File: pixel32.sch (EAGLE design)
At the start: 68 parts, among them CON1 DS1066-07M-SIDE, CON2 DS1066-07M-SIDE, CON3 PINHEAD_1X02-2.54, CON4 PINHEAD_1X01-2.54, CON5 PINHEAD_1X01-2.54, CON6 PINHEAD_1X01-2.54, CON7 PINHEAD_1X01-2.54, IC1 STM32F030K6TX-LQFP32(7X7), IC3 ST3485SOIC8, IC6 MC74VHC1GT125, IC7 MC74VHC1GT125, IC8 LM317

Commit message: blah
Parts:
- added PAD3: WIREPADSMD2.5-1.8, valenok_master_library:WIREPADSMD2.5-1.8
- added U$3: CONNECTION, usb2can_master_lib:CONNECTION
- PAD1, PAD2, PAD4: BOM (none) -> EXCLUDE
- R10: device rc:R-0805 -> rc:R-0603
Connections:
- net CLOCK_BUFFERED: now also RN2.3; no longer RN2.2
- net GND: now also U$3.P$2
- net GNDD: now also U$3.P$1
- net N$15: now also RN2.6; no longer RN2.7
- net VDD_3V3: now also PAD3.P
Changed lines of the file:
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@@
 <attribute name="BOM" x="124.46" y="137.16" size="1.778" layer="96" rot="R180" display="off"/>
 </instance>
-<instance part="TP3" gate="G$1" x="121.92" y="116.84" rot="R180">
-<attribute name="PARTNO" x="121.92" y="116.84" size="1.778" layer="96" rot="R180" display="off"/>
-<attribute name="BOM" x="121.92" y="116.84" size="1.778" layer="96" rot="R180" display="off"/>
+<instance part="TP3" gate="G$1" x="124.46" y="116.84" rot="R180">
+<attribute name="PARTNO" x="124.46" y="116.84" size="1.778" layer="96" rot="R180" display="off"/>
+<attribute name="BOM" x="124.46" y="116.84" size="1.778" layer="96" rot="R180" display="off"/>
 </instance>
 <instance part="Q1" gate="G$1" x="137.16" y="129.54"/>
 <instance part="FRAME1" gate="G$1" x="0" y="0"/>
 <instance part="C1" gate="G$1" x="152.4" y="142.24" rot="R90"/>
-<instance part="TP4" gate="G$1" x="121.92" y="101.6">
-<attribute name="PARTNO" x="121.92" y="101.6" size="1.778" layer="96" display="off"/>
-<attribute name="BOM" x="121.92" y="101.6" size="1.778" layer="96" display="off"/>
-</instance>
-<instance part="GND2" gate="1" x="111.76" y="96.52" rot="MR0"/>
+<instance part="TP4" gate="G$1" x="124.46" y="101.6">
+<attribute name="PARTNO" x="124.46" y="101.6" size="1.778" layer="96" display="off"/>
+<attribute name="BOM" x="124.46" y="101.6" size="1.778" layer="96" display="off"/>
+</instance>
+<instance part="GND2" gate="1" x="114.3" y="96.52" rot="MR0"/>
 </instances>
 <busses>
@@
 <segment>
 <pinref part="GND2" gate="1" pin="GND"/>
-<wire x1="111.76" y1="99.06" x2="111.76" y2="101.6" width="0.1524" layer="91"/>
+<wire x1="114.3" y1="99.06" x2="114.3" y2="101.6" width="0.1524" layer="91"/>
 <pinref part="TP4" gate="G$1" pin="P$1"/>
-<wire x1="111.76" y1="101.6" x2="114.3" y2="101.6" width="0.1524" layer="91"/>
+<wire x1="114.3" y1="101.6" x2="116.84" y2="101.6" width="0.1524" layer="91"/>
 </segment>
 </net>
@@
 <junction x="142.24" y="116.84"/>
 <pinref part="TP3" gate="G$1" pin="P$1"/>
-<wire x1="137.16" y1="116.84" x2="129.54" y2="116.84" width="0.1524" layer="91"/>
+<wire x1="137.16" y1="116.84" x2="132.08" y2="116.84" width="0.1524" layer="91"/>
 <pinref part="Q1" gate="G$1" pin="S"/>
 <wire x1="137.16" y1="124.46" x2="137.16" y2="116.84" width="0.1524" layer="91"/>
@@
 <part name="GND19" library="supply_symbols" deviceset="GND" device="" value="GND"/>
 <part name="+P16" library="supply_symbols" deviceset="24V" device=""/>
-<part name="R10" library="rc" deviceset="R" device="-0805"/>
+<part name="R10" library="rc" deviceset="R" device="-0603"/>
 <part name="R13" library="rc" deviceset="R" device="-0603"/>
 <part name="GND37" library="supply_symbols" deviceset="GND" device="" value="GND"/>
@@
 </part>
 <part name="+P17" library="supply_symbols" deviceset="3.3V" device=""/>
-<part name="PAD1" library="valenok_master_library" deviceset="WIREPAD" device="SMD2.5-1.8"/>
-<part name="PAD2" library="valenok_master_library" deviceset="WIREPAD" device="SMD2.5-1.8"/>
-<part name="PAD4" library="valenok_master_library" deviceset="WIREPAD" device="SMD2.5-1.8"/>
+<part name="PAD1" library="valenok_master_library" deviceset="WIREPAD" device="SMD2.5-1.8">
+<attribute name="BOM" value="EXCLUDE"/>
+</part>
+<part name="PAD2" library="valenok_master_library" deviceset="WIREPAD" device="SMD2.5-1.8">
+<attribute name="BOM" value="EXCLUDE"/>
+</part>
+<part name="PAD4" library="valenok_master_library" deviceset="WIREPAD" device="SMD2.5-1.8">
+<attribute name="BOM" value="EXCLUDE"/>
+</part>
 <part name="GND9" library="supply_symbols" deviceset="GNDD" device="" value="GNDD"/>
 <part name="CON4" library="pinhead" deviceset="PINHEAD_1X01" device="-2.54"/>
@@
 <part name="+P18" library="supply_symbols" deviceset="3.3V" device=""/>
 <part name="U$1" library="logo" deviceset="RTU" device=""/>
+<part name="U$3" library="usb2can_master_lib" deviceset="CONNECTION" device=""/>
+<part name="PAD3" library="valenok_master_library" deviceset="WIREPAD" device="SMD2.5-1.8">
+<attribute name="BOM" value="EXCLUDE"/>
+</part>
 </parts>
 <sheets>
@@
 </instance>
 <instance part="+P17" gate="G$1" x="137.16" y="231.14" rot="MR0"/>
-<instance part="PAD1" gate="G$1" x="129.54" y="220.98"/>
-<instance part="PAD2" gate="G$1" x="132.08" y="208.28" rot="R90"/>
-<instance part="PAD4" gate="G$1" x="132.08" y="198.12" rot="R90"/>
+<instance part="PAD1" gate="G$1" x="129.54" y="220.98">
+<attribute name="BOM" x="129.54" y="220.98" size="1.778" layer="96" display="off"/>
+</instance>
+<instance part="PAD2" gate="G$1" x="132.08" y="208.28" rot="R90">
+<attribute name="BOM" x="132.08" y="208.28" size="1.778" layer="96" rot="R90" display="off"/>
+</instance>
+<instance part="PAD4" gate="G$1" x="132.08" y="198.12" rot="R90">
+<attribute name="BOM" x="132.08" y="198.12" size="1.778" layer="96" rot="R90" display="off"/>
+</instance>
 <instance part="GND9" gate="G$1" x="160.02" y="160.02" rot="MR0"/>
 <instance part="CON4" gate="G$1" x="96.52" y="139.7" rot="R270"/>
@@
 <instance part="CON7" gate="G$1" x="119.38" y="139.7" rot="R270"/>
 <instance part="+P18" gate="G$1" x="109.22" y="190.5"/>
-<instance part="U$1" gate="G$1" x="302.26" y="134.62"/>
+<instance part="U$1" gate="G$1" x="373.38" y="63.5"/>
+<instance part="U$3" gate="G$1" x="335.28" y="167.64" rot="MR0"/>
+<instance part="PAD3" gate="G$1" x="129.54" y="228.6">
+<attribute name="BOM" x="129.54" y="228.6" size="1.778" layer="96" display="off"/>
+</instance>
 </instances>
 <busses>
@@
 <wire x1="139.7" y1="228.6" x2="137.16" y2="228.6" width="0.1524" layer="91"/>
 <wire x1="137.16" y1="228.6" x2="137.16" y2="231.14" width="0.1524" layer="91"/>
+<pinref part="PAD3" gate="G$1" pin="P"/>
+<wire x1="137.16" y1="228.6" x2="132.08" y2="228.6" width="0.1524" layer="91"/>
+<junction x="137.16" y="228.6"/>
 </segment>
 <segment>
@@
 <pinref part="GND44" gate="1" pin="GND"/>
 <wire x1="330.2" y1="165.1" x2="330.2" y2="162.56" width="0.1524" layer="91"/>
+<wire x1="330.2" y1="165.1" x2="330.2" y2="167.64" width="0.1524" layer="91"/>
+<junction x="330.2" y="165.1"/>
+<pinref part="U$3" gate="G$1" pin="P$2"/>
+<wire x1="332.74" y1="167.64" x2="330.2" y2="167.64" width="0.1524" layer="91"/>
 </segment>
 <segment>
@@
 <segment>
 <pinref part="CON2" gate="G$1" pin="5"/>
-<wire x1="327.66" y1="182.88" x2="340.36" y2="182.88" width="0.1524" layer="91"/>
-<pinref part="RN2" gate="G$1" pin="7"/>
+<pinref part="RN2" gate="G$1" pin="6"/>
+<wire x1="330.2" y1="182.88" x2="340.36" y2="182.88" width="0.1524" layer="91"/>
+<wire x1="327.66" y1="180.34" x2="330.2" y2="180.34" width="0.1524" layer="91"/>
+<wire x1="330.2" y1="180.34" x2="330.2" y2="182.88" width="0.1524" layer="91"/>
 </segment>
 </net>
@@
 <pinref part="CON2" gate="G$1" pin="6"/>
 <pinref part="RN2" gate="G$1" pin="5"/>
-<wire x1="330.2" y1="180.34" x2="340.36" y2="180.34" width="0.1524" layer="91"/>
-<wire x1="327.66" y1="177.8" x2="330.2" y2="177.8" width="0.1524" layer="91"/>
-<wire x1="330.2" y1="177.8" x2="330.2" y2="180.34" width="0.1524" layer="91"/>
+<wire x1="332.74" y1="180.34" x2="340.36" y2="180.34" width="0.1524" layer="91"/>
+<wire x1="327.66" y1="177.8" x2="332.74" y2="177.8" width="0.1524" layer="91"/>
+<wire x1="332.74" y1="177.8" x2="332.74" y2="180.34" width="0.1524" layer="91"/>
 </segment>
 </net>
 <net name="CLOCK_BUFFERED" class="0">
 <segment>
-<wire x1="314.96" y1="182.88" x2="312.42" y2="182.88" width="0.1524" layer="91"/>
-<label x="312.42" y="182.88" size="1.27" layer="95" rot="R180" xref="yes"/>
-<pinref part="RN2" gate="G$1" pin="2"/>
+<label x="309.88" y="182.88" size="1.27" layer="95" rot="R180" xref="yes"/>
+<pinref part="RN2" gate="G$1" pin="3"/>
+<wire x1="312.42" y1="182.88" x2="309.88" y2="182.88" width="0.1524" layer="91"/>
+<wire x1="314.96" y1="180.34" x2="312.42" y2="180.34" width="0.1524" layer="91"/>
+<wire x1="312.42" y1="180.34" x2="312.42" y2="182.88" width="0.1524" layer="91"/>
 </segment>
 <segment>
@@
 <pinref part="U$6" gate="G$1" pin="P$1"/>
 <wire x1="340.36" y1="165.1" x2="337.82" y2="165.1" width="0.1524" layer="91"/>
-</segment>
-<segment>
+<pinref part="U$3" gate="G$1" pin="P$1"/>
+<wire x1="337.82" y1="167.64" x2="340.36" y2="167.64" width="0.1524" layer="91"/>
+<wire x1="340.36" y1="167.64" x2="340.36" y2="165.1" width="0.1524" layer="91"/>
+<junction x="340.36" y="165.1"/>
+</segment>
+<segment>

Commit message: -pixel32 update
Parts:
- removed FRAME1: RTU_A4, frames:RTU_A4
- removed FRAME2: RTU_A3, frames:RTU_A3
- added CON10, CON11, CON8, CON9: PINHEAD_1X01-2.54, pinhead:PINHEAD_1X01-2.54
- added CON12: PINHEAD_1X02-2.54, pinhead:PINHEAD_1X02-2.54
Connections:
- net GND: now also CON12.2, CON3.2
- net N$10: now also CON9.1
- net N$21: now also CON10.1
- net N$23: now also CON11.1
- net TEMP: now also CON12.1; no longer R8.2
- net VDD_24V: now also CON8.1
- net VDD_3V3: now also R8.2; no longer CON3.2
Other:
- moved on the sheet: C26, CON3, R8

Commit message: -pixel32 update
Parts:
- removed U$1: RTU, logo:RTU
- added D5: SMBJ26CA-SMB, ExitControl_v2_master_library:SMBJ26CA-SMB
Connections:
- net GND: now also CON12.1, CON3.1, D5.A; no longer CON12.2, CON3.2, R8.1
- net TEMP: now also CON12.2, CON3.2, R8.1; no longer CON12.1, CON3.1
- net VDD_24V: now also D5.C
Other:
- moved on the sheet: C1, C2, C26, C3, C4, C5, CON1, CON2, IC8, MODULE1, R6, R7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

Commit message: -more edge connectors
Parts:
- added CON13, CON14: PINHEAD_1X07-2, pinhead:PINHEAD_1X07-2
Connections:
- net GNDD: now also CON13.1, CON14.1
- net N$11: now also CON13.4
- net N$12: now also CON13.3
- net N$13: now also CON13.2
- net N$14: now also CON14.4
- net N$15: now also CON14.3
- net N$19: now also CON14.2
- net RS485_A: now also CON13.6, CON14.6
- net RS485_B: now also CON13.5, CON14.5
- net VDD_24V: now also CON13.7, CON14.7
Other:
- moved on the sheet: CON1, CON2, D5

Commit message: voltage regulator recalculated, minor fixes, attributes
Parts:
- removed Z1: 16MHz, watchdog_master_library:CRYSTAL-3.2X2.5-4P
- added C6: 100 nF, rc:C-0603
- added Y1: 16MHz, crystals:CRYSTAL-3.2X2.5-4P
- C1, C16, C2, C3, C4: FARNELL# (none) -> 2496930
- C13, C17, C18, C23, C24, C26: FARNELL# (none) -> 2496834
- C14: FARNELL# (none) -> 2496917
- C15: FARNELL# (none) -> 2496827
- C19, C20: value (none) -> 10 pF; FARNELL# (none) -> 1414601
- C21: value 0.1uF -> 100 nF; FARNELL# (none) -> 2496834
- C5: value (none) -> 10 uF
- CON1, CON2: value DS1066-07M-SIDE -> B7B-PH-K-S-SIDE; device pixel_masterlib:DS1066-07M-SIDE -> pixel_masterlib:B7B-PH-K-S-SIDE
- D5: value SMBJ26CA-SMB -> TVS_DIODE-SMB; device ExitControl_v2_master_library:SMBJ26CA-SMB -> pixel_masterlib:TVS_DIODE-SMB; CHIPDIP (none) -> 8023193826; DIGIKEY# (none) -> 497-15658-2-ND; FARNELL# (none) -> 1749366; MANF (none) -> STMicroelectronics; MANF# (none) -> SMBJ26CA; TME# (none) -> SMBJ26CA
- IC8: device masterlib:LM317 -> pixel_masterlib:LM317
- LED2: CHIPDIP (none) -> 8598509892; FARNELL# (none) -> 2293494; TME# (none) -> LTST-C191KGKT
- LED_ANODE, LED_CATHODE1, LED_CATHODE2, LED_CATHODE3: value WIREPADSMD5-2,5 -> WIREPADSMD2.5-1.8; device valenok_master_library:WIREPADSMD5-2,5 -> wirepad:WIREPADSMD2.5-1.8
- MODULE1: device ali_modules:GW1584 -> pixel_masterlib:GW1584
- PAD1, PAD2, PAD3, PAD4: device valenok_master_library:WIREPADSMD2.5-1.8 -> wirepad:WIREPADSMD2.5-1.8
- R1, R2: ASSY DO NOT PLACE -> DO NOT MOUNT
- R11, R12: FARNELL# (none) -> 2303059
- R14, R15, R8, R9: FARNELL# (none) -> 2008341
- R39: FARNELL# (none) -> 2303145
- R5: FARNELL# (none) -> 2303067
- R6: device rc:R-0805 -> rc:R-0603; FARNELL# (none) -> 2303145
- R7: value 5K6 -> 1K6; device rc:R-0805 -> rc:R-0603; FARNELL# (none) -> 2303159
- SJ1, SJ2, SJ3, SJ4: BOM (none) -> EXCLUDE
- TP1, TP2, TP3, TP4: device pixhawk2:PAD.05 -> misc:PAD.05
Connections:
- net GND: now also C6.1, Y1.GND; no longer Z1.GND
- net N$4: now also Y1.1; no longer Z1.1
- net N$5: now also C6.2
- net N$9: now also Y1.2; no longer Z1.2
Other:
- note added: "10 uF 50V in 1812 packagage is unavailable"
- note added: "Crystal load capacitance is 9 pF, otherwise recalculate C19 and C20"
- note added: "Do not mount"
- note added: "No 510 Ohm resistor arrays are available on Farnell nor TME"
- note added: "R1, R2 are for software version definition"
- note added: "R10, R13 are not defined"
- note added: "RGB LED SINGLE CHANNEL"
- note removed: "Do not use"
- note removed: "R1, R2, R3 are for software version definition"
- note removed: "RGB LED RED CHANNEL"
- moved on the sheet: C19, C20, C21, C23, C24, C26, C5, CON1, CON12, CON2, CON3, D1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

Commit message: input sense divider values added boot0 fix
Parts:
- added R3: 20K, rc:R-0603
- R10: value (none) -> 100K
- R13: value (none) -> 10K
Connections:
- new net N$6: IC1.PB8, R3.1
- net GND: now also R3.2
- net N$3: now also R3.2
- net PWM: now also R3.1

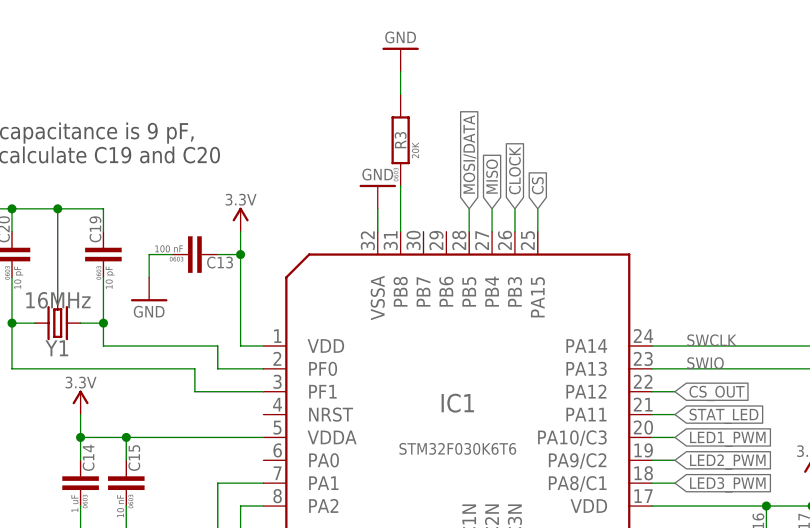
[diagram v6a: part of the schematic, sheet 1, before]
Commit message: TME part numbers added
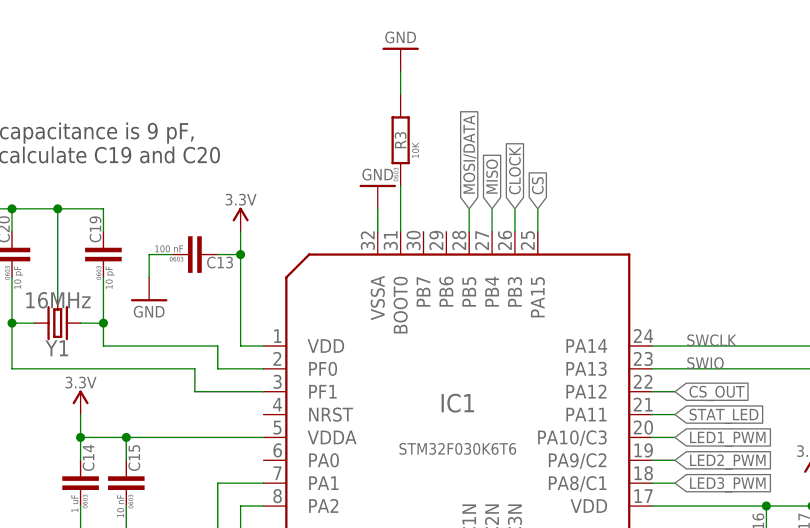
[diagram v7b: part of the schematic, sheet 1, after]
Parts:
- C1, C16, C2, C3, C4: TME# (none) -> GRM188R60J475KE19D
- C13, C17, C18, C21, C23, C24, C26, C6: TME# (none) -> GRM188R71H104KA93D
- C14: TME# (none) -> GRM188R61C105KA93D
- C15: TME# (none) -> C0603C103K3RACTU
- C19, C20: TME# (none) -> GRM1885C1H100JA01D
- C5: FARNELL# (none) -> 2449143; TME# (none) -> CL32B106KBJNNNE
- D5: CHIPDIP 8023193826 -> (none); CHIPDIP# (none) -> 8023193826
- LED2: CHIPDIP 8598509892 -> (none); CHIPDIP# (none) -> 8598509892
- LED_ANODE, LED_CATHODE1, LED_CATHODE2, LED_CATHODE3: BOM (none) -> EXCLUDE
- R10: FARNELL# (none) -> 2303232; TME# (none) -> RC0603FR-07100KL
- R11, R12: TME# (none) -> RC0603FR-07100RL
- R13: FARNELL# (none) -> 2008341; TME# (none) -> RC0603FR-0710KL
- R14, R15, R8, R9: TME# (none) -> RC0603FR-0710KL
- R3: value 20K -> 10K; FARNELL# (none) -> 2008341; TME# (none) -> RC0603FR-0710KL
- R39, R6: TME# (none) -> RC0603FR-071KL
- R5: TME# (none) -> CRCW0603120RFKTABC
- R7: TME# (none) -> RC0603FR-071K6L
- RN1, RN2: CHIPDIP# (none) -> 9000044911; FARNELL# (none) -> 2321730
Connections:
- net N$6: now also IC1.BOOT0; no longer IC1.PB8
